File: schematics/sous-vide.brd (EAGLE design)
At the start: 81.3 x 81.3 mm, 31 parts, among them IC1 MEGA8-P, T1 BC547, T2 BC547, T3 BC547

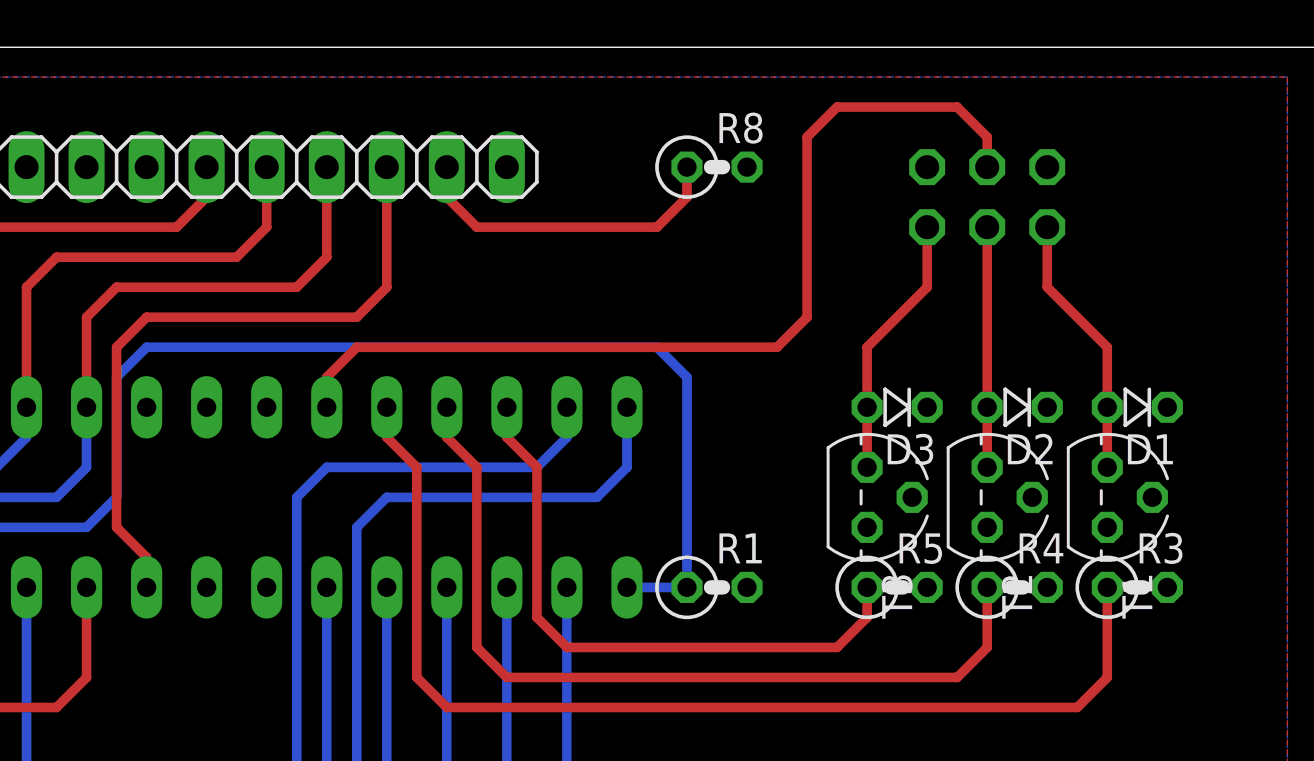
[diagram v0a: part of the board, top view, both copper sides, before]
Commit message: Minor shift in components.
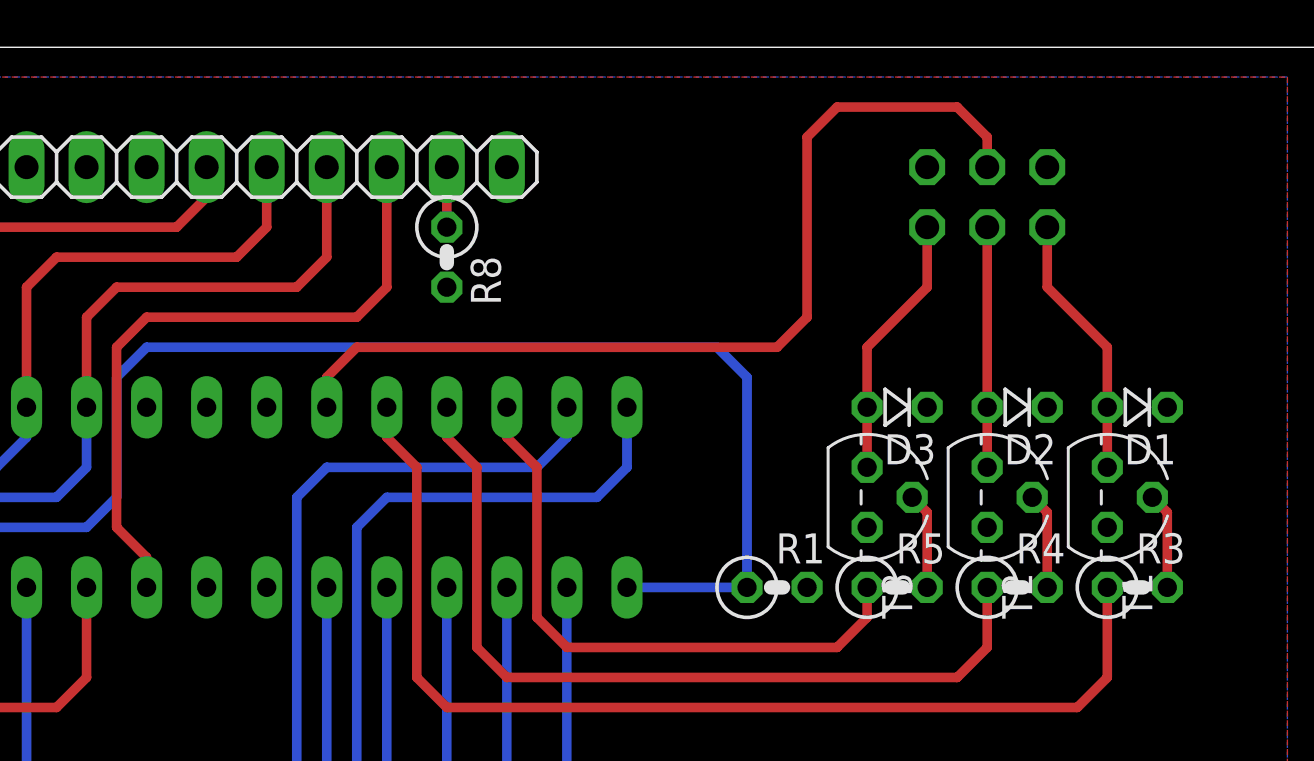
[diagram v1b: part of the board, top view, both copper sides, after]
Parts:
- moved R8 12.0 mm to (44.5, 72.4), turned to 270 degrees
- moved R1 2.54 mm to (58.4, 58.4)
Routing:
- net N$15: track 13.8 -> 2.54 mm
- net N$31: track 62.3 -> 67.4 mm
- net N$10: track 0.00 -> 4.07 mm
- net N$12: track 0.00 -> 4.07 mm
- net N$11: track 0.00 -> 4.07 mm
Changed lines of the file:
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@@
 </autorouter>
 <elements>
-<element name="R1" library="rcl" package="0207/2V" value="100k" x="55.88" y="58.42"/>
+<element name="R1" library="rcl" package="0207/2V" value="100k" x="58.42" y="58.42"/>
 <element name="JP3" library="pinhead" package="1X16" value="display" x="27.94" y="76.2"/>
 <element name="S7" library="switch-misc" package="DT6" value="DT6" x="67.31" y="35.56"/>
@@
 <element name="R6" library="rcl" package="0207/2V" value="330" x="26.67" y="27.94"/>
 <element name="R7" library="resistor" package="RTRIM3339P" value="" x="11.43" y="69.85" rot="R90"/>
-<element name="R8" library="rcl" package="0207/2V" value="330" x="55.88" y="76.2"/>
+<element name="R8" library="rcl" package="0207/2V" value="330" x="44.45" y="72.39" rot="R270"/>
 <element name="H1" library="holes" package="3,0" value="MOUNT-HOLE3.0" x="76.2" y="5.08"/>
 <element name="H2" library="holes" package="3,0" value="MOUNT-HOLE3.0" x="5.08" y="40.64"/>
@@
 <contactref element="R8" pad="1"/>
 <contactref element="JP3" pad="15"/>
-<wire x1="54.61" y1="76.2" x2="54.61" y2="74.93" width="0.4064" layer="1"/>
-<wire x1="54.61" y1="74.93" x2="53.34" y2="73.66" width="0.4064" layer="1"/>
-<wire x1="53.34" y1="73.66" x2="45.72" y2="73.66" width="0.4064" layer="1"/>
-<wire x1="45.72" y1="73.66" x2="44.45" y2="74.93" width="0.4064" layer="1"/>
-<wire x1="44.45" y1="74.93" x2="44.45" y2="76.2" width="0.4064" layer="1"/>
+<wire x1="44.45" y1="76.2" x2="44.45" y2="73.66" width="0.4064" layer="1"/>
 </signal>
 <signal name="N$26">
@@
 <wire x1="30.48" y1="62.23" x2="30.48" y2="67.31" width="0.4064" layer="16"/>
 <wire x1="30.48" y1="67.31" x2="31.75" y2="68.58" width="0.4064" layer="16"/>
-<wire x1="31.75" y1="68.58" x2="53.34" y2="68.58" width="0.4064" layer="16"/>
-<wire x1="53.34" y1="68.58" x2="54.61" y2="67.31" width="0.4064" layer="16"/>
+<wire x1="31.75" y1="68.58" x2="55.88" y2="68.58" width="0.4064" layer="16"/>
+<wire x1="55.88" y1="68.58" x2="57.15" y2="67.31" width="0.4064" layer="16"/>
 <wire x1="11.43" y1="58.42" x2="15.24" y2="58.42" width="0.4064" layer="16"/>
 <wire x1="15.24" y1="58.42" x2="17.78" y2="60.96" width="0.4064" layer="16"/>
 <contactref element="IC1" pad="1"/>
 <contactref element="R1" pad="1"/>
-<wire x1="52.07" y1="58.42" x2="54.61" y2="58.42" width="0.4064" layer="16"/>
-<wire x1="54.61" y1="58.42" x2="54.61" y2="67.31" width="0.4064" layer="16"/>
+<wire x1="52.07" y1="58.42" x2="57.15" y2="58.42" width="0.4064" layer="16"/>
+<wire x1="57.15" y1="58.42" x2="57.15" y2="67.31" width="0.4064" layer="16"/>
 </signal>
 <signal name="N$8">
@@
 <contactref element="R3" pad="2"/>
 <contactref element="T1" pad="2"/>
-<wire x1="74.93" y1="58.42" x2="74.295" y2="62.23" width="0" layer="19" extent="1-1"/>
+<wire x1="74.93" y1="58.42" x2="74.93" y2="61.595" width="0.4064" layer="1"/>
+<wire x1="74.93" y1="61.595" x2="74.295" y2="62.23" width="0.4064" layer="1"/>
 </signal>
 <signal name="N$11">
 <contactref element="R4" pad="2"/>
 <contactref element="T2" pad="2"/>
-<wire x1="69.85" y1="58.42" x2="69.215" y2="62.23" width="0" layer="19" extent="1-1"/>
+<wire x1="69.85" y1="58.42" x2="69.85" y2="61.595" width="0.4064" layer="1"/>
+<wire x1="69.85" y1="61.595" x2="69.215" y2="62.23" width="0.4064" layer="1"/>
 </signal>
 <signal name="N$12">
 <contactref element="R5" pad="2"/>
 <contactref element="T3" pad="2"/>
-<wire x1="64.77" y1="58.42" x2="64.135" y2="62.23" width="0" layer="19" extent="1-1"/>
+<wire x1="64.77" y1="58.42" x2="64.77" y2="61.595" width="0.4064" layer="1"/>
+<wire x1="64.77" y1="61.595" x2="64.135" y2="62.23" width="0.4064" layer="1"/>
 </signal>
 <signal name="N$13">

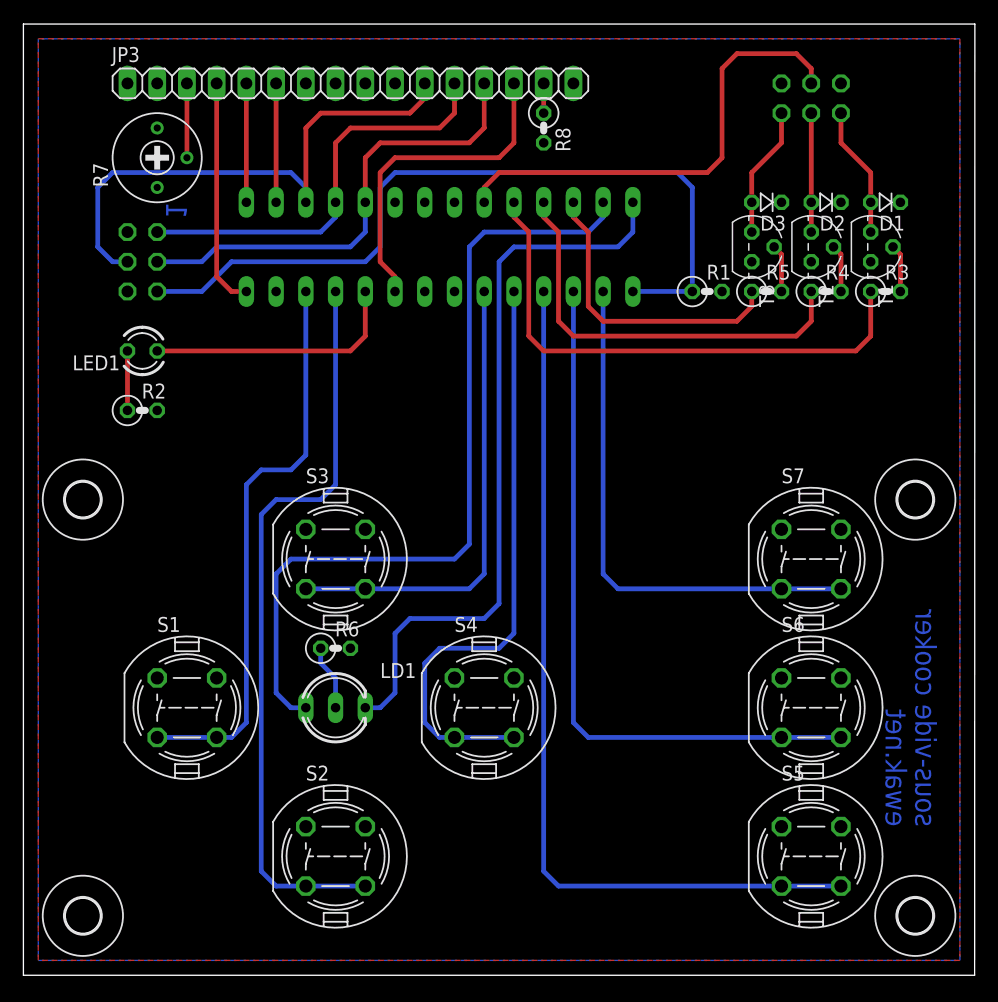
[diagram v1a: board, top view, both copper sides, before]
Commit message: minor tweaks in component placement, sent to pcb manufacturer
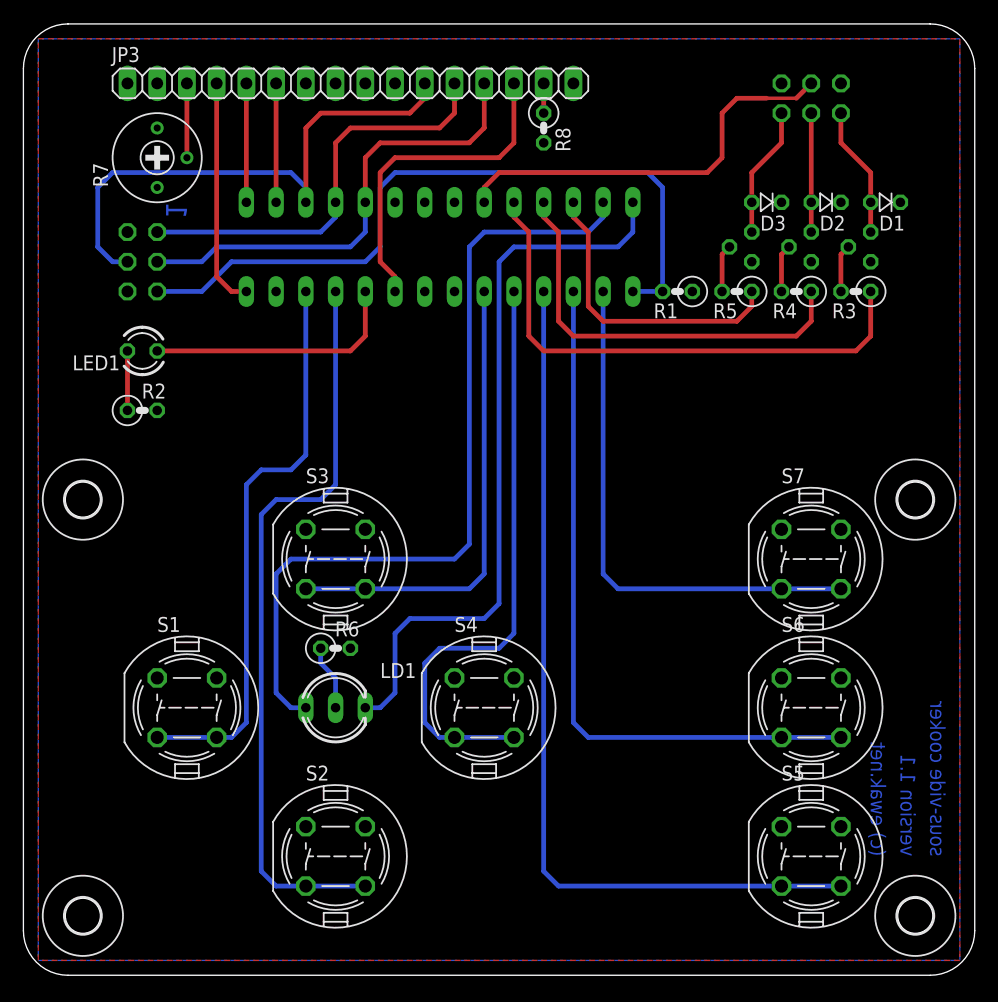
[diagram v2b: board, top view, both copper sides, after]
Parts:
- JP2: value ISP -> IO
- moved R1 2.54 mm to (55.9, 58.4), turned to 180 degrees
- moved R5 2.54 mm to (61.0, 58.4), turned to 180 degrees
- moved R3 2.54 mm to (71.1, 58.4), turned to 180 degrees
- moved R4 2.54 mm to (66.0, 58.4), turned to 180 degrees
- flipped T1 to the bottom
- flipped T2 to the bottom
- flipped T3 to the bottom
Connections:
- net N$31: now also R1.2; no longer R1.1
- net VCC: now also R1.1; no longer R1.2
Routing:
- net N$31: track 67.4 -> 62.3 mm
- net N$3: track 40.2 -> 35.1 mm
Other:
- outline, holes or cut-outs redrawn
- board text added: "(c) ewak.net"
- board text added: "version 1.1"
- board text removed: "ewak.net"
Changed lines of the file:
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@@
 <board>
 <plain>
-<wire x1="0" y1="0" x2="81.27" y2="0" width="0" layer="20"/>
-<wire x1="81.27" y1="0" x2="81.29" y2="81.27" width="0" layer="20"/>
-<wire x1="81.29" y1="81.27" x2="0" y2="81.27" width="0" layer="20"/>
-<wire x1="0" y1="81.27" x2="0" y2="0" width="0" layer="20"/>
-<text x="76.2" y="12.7" size="1.778" layer="16" rot="MR90">sous-vide cooker</text>
-<text x="73.66" y="12.7" size="1.778" layer="16" rot="MR90">ewak.net</text>
+<wire x1="3.81" y1="0" x2="77.47" y2="0" width="0" layer="20"/>
 <text x="13.97" y="66.04" size="1.778" layer="16" rot="MR270">1</text>
+<text x="77.47" y="10.16" size="1.27" layer="16" font="vector" rot="MR90">sous-vide cooker</text>
+<text x="74.93" y="10.16" size="1.27" layer="16" font="vector" rot="MR90">version 1.1</text>
+<text x="72.39" y="10.16" size="1.27" layer="16" font="vector" rot="MR90">(c) ewak.net</text>
+<wire x1="0" y1="77.47" x2="0" y2="3.81" width="0" layer="20"/>
+<wire x1="0" y1="77.47" x2="3.81" y2="81.28" width="0" layer="20" curve="-90"/>
+<wire x1="0" y1="3.81" x2="3.81" y2="0" width="0" layer="20" curve="90"/>
+<wire x1="77.47" y1="0" x2="81.28" y2="3.81" width="0" layer="20" curve="90"/>
+<wire x1="77.47" y1="81.28" x2="81.28" y2="77.47" width="0" layer="20" curve="-90"/>
+<wire x1="81.28" y1="3.81" x2="81.28" y2="77.47" width="0" layer="20"/>
+<wire x1="3.81" y1="81.28" x2="77.47" y2="81.28" width="0" layer="20"/>
 </plain>
 <attributes>
@@
 </autorouter>
 <elements>
-<element name="R1" library="rcl" package="0207/2V" value="100k" x="58.42" y="58.42"/>
+<element name="R1" library="rcl" package="0207/2V" value="100k" x="55.88" y="58.42" rot="R180"/>
 <element name="JP3" library="pinhead" package="1X16" value="display" x="27.94" y="76.2"/>
 <element name="S7" library="switch-misc" package="DT6" value="DT6" x="67.31" y="35.56"/>
@@
 <element name="LED1" library="led" package="LED3MM" value="" x="10.16" y="53.34" rot="R180"/>
 <element name="R2" library="rcl" package="0207/2V" value="330" x="10.16" y="48.26"/>
-<element name="T2" library="transistor" package="TO92" value="BC547" x="67.31" y="62.23" rot="R270"/>
-<element name="T3" library="transistor" package="TO92" value="BC547" x="62.23" y="62.23" rot="R270"/>
-<element name="T1" library="transistor" package="TO92" value="BC547" x="72.39" y="62.23" rot="R270"/>
+<element name="T2" library="transistor" package="TO92" value="BC547" x="67.31" y="62.23" rot="MR270"/>
+<element name="T3" library="transistor" package="TO92" value="BC547" x="62.23" y="62.23" rot="MR270"/>
+<element name="T1" library="transistor" package="TO92" value="BC547" x="72.39" y="62.23" rot="MR270"/>
 <element name="D1" library="diode" package="D-2.5" value="" x="73.66" y="66.04" rot="R180"/>
 <element name="D2" library="diode" package="D-2.5" value="" x="68.58" y="66.04" rot="R180"/>
 <element name="D3" library="diode" package="D-2.5" value="" x="63.5" y="66.04" rot="R180"/>
-<element name="R3" library="rcl" package="0207/2V" value="330" x="73.66" y="58.42"/>
-<element name="R4" library="rcl" package="0207/2V" value="330" x="68.58" y="58.42"/>
-<element name="R5" library="rcl" package="0207/2V" value="330" x="63.5" y="58.42"/>
-<element name="JP2" library="pinhead" package="2X03" value="ISP" x="67.31" y="74.93" rot="MR180"/>
+<element name="R3" library="rcl" package="0207/2V" value="330" x="71.12" y="58.42" rot="R180"/>
+<element name="R4" library="rcl" package="0207/2V" value="330" x="66.04" y="58.42" rot="R180"/>
+<element name="R5" library="rcl" package="0207/2V" value="330" x="60.96" y="58.42" rot="R180"/>
+<element name="JP2" library="pinhead" package="2X03" value="IO" x="67.31" y="74.93" rot="MR180"/>
 </elements>
 <signals>
@@
 <contactref element="IC1" pad="20"/>
 <contactref element="IC1" pad="21"/>
-<contactref element="R1" pad="2"/>
 <contactref element="JP2" pad="1"/>
 <contactref element="D3" pad="C"/>
 <contactref element="D2" pad="C"/>
 <contactref element="D1" pad="C"/>
+<contactref element="R1" pad="1"/>
 </signal>
 <signal name="N$14">
@@
 <wire x1="30.48" y1="62.23" x2="30.48" y2="67.31" width="0.4064" layer="16"/>
 <wire x1="30.48" y1="67.31" x2="31.75" y2="68.58" width="0.4064" layer="16"/>
-<wire x1="31.75" y1="68.58" x2="55.88" y2="68.58" width="0.4064" layer="16"/>
-<wire x1="55.88" y1="68.58" x2="57.15" y2="67.31" width="0.4064" layer="16"/>
+<wire x1="31.75" y1="68.58" x2="53.34" y2="68.58" width="0.4064" layer="16"/>
 <wire x1="11.43" y1="58.42" x2="15.24" y2="58.42" width="0.4064" layer="16"/>
 <wire x1="15.24" y1="58.42" x2="17.78" y2="60.96" width="0.4064" layer="16"/>
+<contactref element="R1" pad="2"/>
 <contactref element="IC1" pad="1"/>
-<contactref element="R1" pad="1"/>
-<wire x1="52.07" y1="58.42" x2="57.15" y2="58.42" width="0.4064" layer="16"/>
-<wire x1="57.15" y1="58.42" x2="57.15" y2="67.31" width="0.4064" layer="16"/>
+<wire x1="52.07" y1="58.42" x2="54.61" y2="58.42" width="0.4064" layer="16"/>
+<wire x1="54.61" y1="58.42" x2="54.61" y2="67.31" width="0.4064" layer="16"/>
+<wire x1="54.61" y1="67.31" x2="53.34" y2="68.58" width="0.4064" layer="16"/>
 </signal>
 <signal name="N$8">
@@
 <contactref element="IC1" pad="23"/>
 <contactref element="JP2" pad="3"/>
-<wire x1="67.31" y1="76.2" x2="67.31" y2="77.47" width="0.4064" layer="1"/>
-<wire x1="67.31" y1="77.47" x2="66.04" y2="78.74" width="0.4064" layer="1"/>
-<wire x1="66.04" y1="78.74" x2="60.96" y2="78.74" width="0.4064" layer="1"/>
-<wire x1="60.96" y1="78.74" x2="59.69" y2="77.47" width="0.4064" layer="1"/>
-<wire x1="59.69" y1="77.47" x2="59.69" y2="69.85" width="0.4064" layer="1"/>
 <wire x1="59.69" y1="69.85" x2="58.42" y2="68.58" width="0.4064" layer="1"/>
 <wire x1="58.42" y1="68.58" x2="40.64" y2="68.58" width="0.4064" layer="1"/>
 <wire x1="40.64" y1="68.58" x2="39.37" y2="67.31" width="0.4064" layer="1"/>
 <wire x1="39.37" y1="67.31" x2="39.37" y2="66.04" width="0.4064" layer="1"/>
+<wire x1="59.69" y1="69.85" x2="59.69" y2="73.66" width="0.4064" layer="1"/>
+<wire x1="59.69" y1="73.66" x2="60.96" y2="74.93" width="0.4064" layer="1"/>
+<wire x1="66.04" y1="74.93" x2="67.31" y2="76.2" width="0.4064" layer="1"/>
+<wire x1="60.96" y1="74.93" x2="63.5" y2="74.93" width="0.4064" layer="1"/>
+<wire x1="63.5" y1="74.93" x2="66.04" y2="74.93" width="0.3048" layer="1"/>
 </signal>
 <signal name="N$7">
@@
 <wire x1="45.72" y1="55.88" x2="46.99" y2="54.61" width="0.4064" layer="1"/>
 <wire x1="46.99" y1="54.61" x2="66.04" y2="54.61" width="0.4064" layer="1"/>
-<wire x1="66.04" y1="54.61" x2="67.31" y2="55.88" width="0.4064" layer="1"/>
-<wire x1="67.31" y1="55.88" x2="67.31" y2="58.42" width="0.4064" layer="1"/>
+<wire x1="67.31" y1="58.42" x2="67.31" y2="55.88" width="0.4064" layer="1"/>
+<wire x1="67.31" y1="55.88" x2="66.04" y2="54.61" width="0.4064" layer="1"/>
 </signal>
 <signal name="N$6">
@@
 <contactref element="R3" pad="2"/>
 <contactref element="T1" pad="2"/>
-<wire x1="74.93" y1="58.42" x2="74.93" y2="61.595" width="0.4064" layer="1"/>
-<wire x1="74.93" y1="61.595" x2="74.295" y2="62.23" width="0.4064" layer="1"/>
+<wire x1="69.85" y1="58.42" x2="69.85" y2="61.595" width="0.4064" layer="1"/>
+<wire x1="69.85" y1="61.595" x2="70.485" y2="62.23" width="0.4064" layer="1"/>
 </signal>
 <signal name="N$11">
 <contactref element="R4" pad="2"/>
 <contactref element="T2" pad="2"/>
-<wire x1="69.85" y1="58.42" x2="69.85" y2="61.595" width="0.4064" layer="1"/>
-<wire x1="69.85" y1="61.595" x2="69.215" y2="62.23" width="0.4064" layer="1"/>
+<wire x1="64.77" y1="58.42" x2="64.77" y2="61.595" width="0.4064" layer="1"/>
+<wire x1="64.77" y1="61.595" x2="65.405" y2="62.23" width="0.4064" layer="1"/>
 </signal>
 <signal name="N$12">
 <contactref element="R5" pad="2"/>
 <contactref element="T3" pad="2"/>
-<wire x1="64.77" y1="58.42" x2="64.77" y2="61.595" width="0.4064" layer="1"/>
-<wire x1="64.77" y1="61.595" x2="64.135" y2="62.23" width="0.4064" layer="1"/>
+<wire x1="59.69" y1="58.42" x2="59.69" y2="61.595" width="0.4064" layer="1"/>
+<wire x1="59.69" y1="61.595" x2="60.325" y2="62.23" width="0.4064" layer="1"/>
 </signal>
 <signal name="N$13">
@@
 <contactref element="JP2" pad="6"/>
 <contactref element="D1" pad="A"/>
-<wire x1="72.39" y1="63.5" x2="72.39" y2="66.04" width="0.4064" layer="1"/>
 <wire x1="72.39" y1="66.04" x2="72.39" y2="68.58" width="0.4064" layer="1"/>
 <wire x1="72.39" y1="68.58" x2="69.85" y2="71.12" width="0.4064" layer="1"/>
 <wire x1="69.85" y1="71.12" x2="69.85" y2="73.66" width="0.4064" layer="1"/>
+<wire x1="72.39" y1="66.04" x2="72.39" y2="63.5" width="0.4064" layer="1"/>
 </signal>
 <signal name="N$16">
@@
 <contactref element="JP2" pad="2"/>
 <contactref element="D3" pad="A"/>
-<wire x1="62.23" y1="66.04" x2="62.23" y2="63.5" width="0.4064" layer="1"/>
 <wire x1="64.77" y1="73.66" x2="64.77" y2="71.12" width="0.4064" layer="1"/>
 <wire x1="64.77" y1="71.12" x2="62.23" y2="68.58" width="0.4064" layer="1"/>
 <wire x1="62.23" y1="68.58" x2="62.23" y2="66.04" width="0.4064" layer="1"/>
+<wire x1="62.23" y1="66.04" x2="62.23" y2="63.5" width="0.4064" layer="1"/>
 </signal>
 </signals>
